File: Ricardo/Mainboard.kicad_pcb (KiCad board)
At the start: 4 copper layers, 100 x 60 mm, 326 parts, among them J1 USB_B_Micro, J10 Conn_01x02_Male, J11 Conn_01x02_Male, J12 Conn_01x02_Male, J2 8P8C_LED, J3 Micro_SD_Card_Det, J4 Conn_Coaxial, J5 Conn_Coaxial, J6 Screw_Terminal_01x02, J7 Screw_Terminal_01x02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

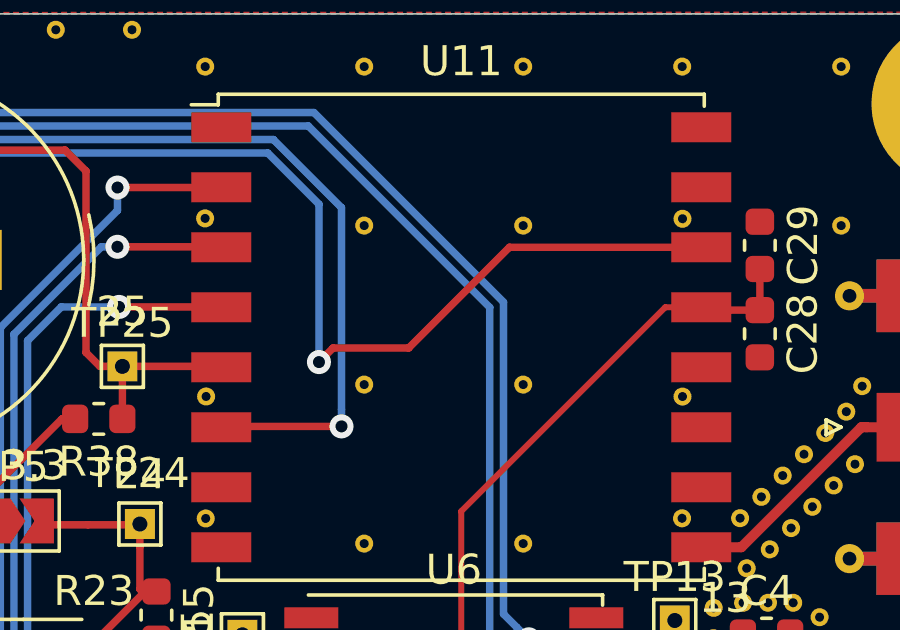
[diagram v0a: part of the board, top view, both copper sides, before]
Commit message: Added mit logo to ricardo board. added wipe functionality to storage controller
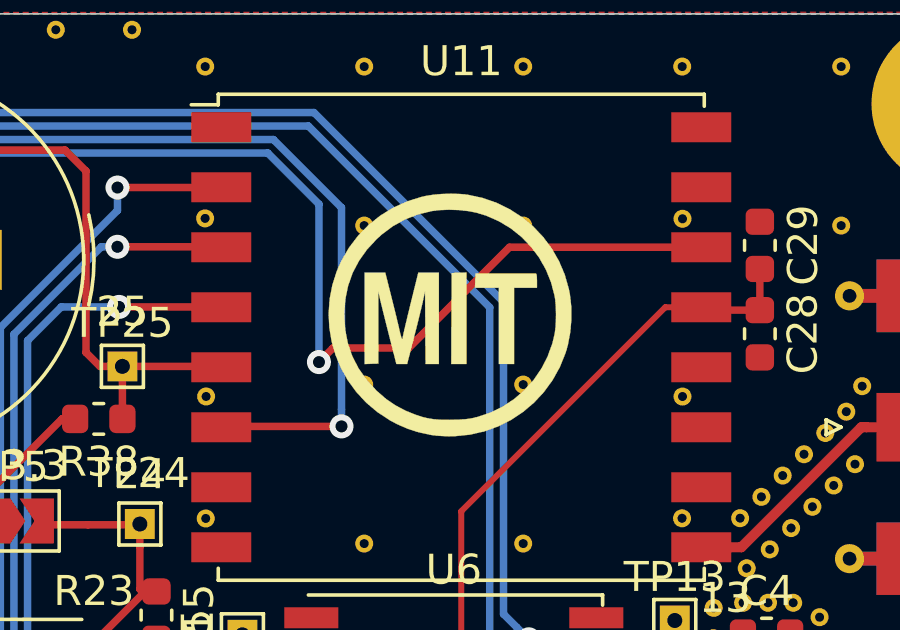
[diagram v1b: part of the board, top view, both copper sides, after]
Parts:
- added G***: LOGO, iclr-hw:MIT_logo, F.Cu at (165.2, 60.0)
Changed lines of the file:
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@@
     (tracks 1316)
     (zones 0)
-    (modules 326)
+    (modules 327)
     (nets 144)
   )
@@
     (uvia_drill 0.1)
   )
+  (module iclr-hw:MIT_logo (layer F.Cu)
+    (at 165.16 60.02)
+    (fp_text reference G*** (at 0 0) (layer F.SilkS) hide
+      (effects (font (size 1.524 1.524) (thickness 0.3)))
+    )
+    (fp_text value LOGO (at -0.05 5.77) (layer F.SilkS) hide
+      (effects (font (size 1.524 1.524) (thickness 0.3)))
+    )
+    (fp_poly (pts (xy 1.833562 -1.366762) (xy 2.079108 -1.366608) (xy 2.304556 -1.36644) (xy 2.501975 -1.366266)
+      (xy 2.663434 -1.366093) (xy 2.781 -1.36593) (xy 2.846742 -1.365785) (xy 2.8575 -1.365724)
+      (xy 2.873462 -1.335939) (xy 2.884619 -1.255889) (xy 2.889217 -1.138736) (xy 2.88925 -1.127125)
+      (xy 2.88925 -0.889) (xy 2.12725 -0.889) (xy 2.12725 1.651) (xy 1.61925 1.651)
+      (xy 1.61925 -0.889) (xy 0.822828 -0.889) (xy 0.832101 -1.128163) (xy 0.841375 -1.367325)
+      (xy 1.833562 -1.366762)) (layer F.SilkS) (width 0.01))
+    (fp_poly (pts (xy 0.53975 1.651) (xy 0.031134 1.651) (xy 0.039379 0.134937) (xy 0.047625 -1.381125)
+      (xy 0.293687 -1.390399) (xy 0.53975 -1.399672) (xy 0.53975 1.651)) (layer F.SilkS) (width 0.01))
+    (fp_poly (pts (xy -0.723536 -1.397) (xy -0.381 -1.397) (xy -0.381 1.651) (xy -0.824746 1.651)
+      (xy -0.833061 0.436562) (xy -0.841375 -0.777875) (xy -0.909244 -0.460375) (xy -0.935357 -0.344657)
+      (xy -0.974623 -0.179146) (xy -1.024176 0.0245) (xy -1.081154 0.254628) (xy -1.142694 0.499581)
+      (xy -1.205934 0.747703) (xy -1.207567 0.754062) (xy -1.438022 1.651) (xy -1.797534 1.651)
+      (xy -2.042334 0.690562) (xy -2.106115 0.439322) (xy -2.167533 0.195524) (xy -2.224052 -0.030632)
+      (xy -2.273139 -0.228944) (xy -2.312259 -0.389211) (xy -2.338878 -0.50123) (xy -2.34404 -0.523875)
+      (xy -2.400948 -0.777875) (xy -2.399037 0.428625) (xy -2.397125 1.635125) (xy -2.627313 1.644453)
+      (xy -2.8575 1.653781) (xy -2.8575 -1.397) (xy -2.167897 -1.397) (xy -1.953853 -0.547688)
+      (xy -1.894471 -0.310563) (xy -1.837603 -0.080676) (xy -1.78593 0.130918) (xy -1.742133 0.313163)
+      (xy -1.708895 0.455007) (xy -1.690063 0.53975) (xy -1.659757 0.669292) (xy -1.631356 0.763619)
+      (xy -1.607866 0.815801) (xy -1.592292 0.818904) (xy -1.58752 0.776287) (xy -1.580113 0.731638)
+      (xy -1.559064 0.632992) (xy -1.526149 0.487956) (xy -1.48314 0.304133) (xy -1.431812 0.089128)
+      (xy -1.373939 -0.149454) (xy -1.326806 -0.341313) (xy -1.066072 -1.397001) (xy -0.723536 -1.397)) (layer F.SilkS) (width 0.01))
+    (fp_poly (pts (xy 0.319577 -4.016704) (xy 0.57754 -3.991174) (xy 0.589705 -3.989348) (xy 1.080211 -3.88321)
+      (xy 1.546617 -3.720879) (xy 1.985107 -3.506085) (xy 2.391865 -3.242561) (xy 2.763073 -2.934037)
+      (xy 3.094917 -2.584246) (xy 3.383579 -2.196918) (xy 3.625244 -1.775785) (xy 3.816096 -1.324579)
+      (xy 3.952318 -0.84703) (xy 3.987706 -0.66675) (xy 4.033388 -0.257684) (xy 4.036025 0.173336)
+      (xy 3.997107 0.606492) (xy 3.918123 1.021965) (xy 3.840837 1.288573) (xy 3.650674 1.755648)
+      (xy 3.409658 2.188464) (xy 3.122002 2.584018) (xy 2.791919 2.939307) (xy 2.423622 3.251329)
+      (xy 2.021322 3.517079) (xy 1.589233 3.733555) (xy 1.131567 3.897754) (xy 0.652537 4.006673)
+      (xy 0.156355 4.057309) (xy -0.047625 4.060557) (xy -0.222552 4.055179) (xy -0.404296 4.043267)
+      (xy -0.565288 4.02688) (xy -0.635 4.016705) (xy -1.045097 3.929237) (xy -1.418609 3.810782)
+      (xy -1.778169 3.653278) (xy -2.020116 3.52328) (xy -2.436011 3.249745) (xy -2.807948 2.934222)
+      (xy -3.134438 2.581634) (xy -3.413992 2.196905) (xy -3.64512 1.78496) (xy -3.826334 1.350721)
+      (xy -3.956145 0.899114) (xy -4.033064 0.435061) (xy -4.052337 0.03175) (xy -3.532943 0.03175)
+      (xy -3.50245 0.508677) (xy -3.414685 0.958777) (xy -3.26904 1.383456) (xy -3.064905 1.784118)
+      (xy -2.801672 2.162168) (xy -2.478732 2.51901) (xy -2.43764 2.558845) (xy -2.138278 2.818013)
+      (xy -1.824742 3.032351) (xy -1.480521 3.21193) (xy -1.1459 3.34677) (xy -0.934756 3.41556)
+      (xy -0.733107 3.464313) (xy -0.524236 3.495268) (xy -0.291425 3.510669) (xy -0.017955 3.512754)
+      (xy 0.079375 3.51101) (xy 0.298106 3.504232) (xy 0.470868 3.493788) (xy 0.615165 3.477699)
+      (xy 0.748505 3.453988) (xy 0.888396 3.420678) (xy 0.895534 3.418815) (xy 1.337238 3.271201)
+      (xy 1.750323 3.06936) (xy 2.130777 2.817604) (xy 2.474586 2.520247) (xy 2.777734 2.181601)
+      (xy 3.03621 1.805979) (xy 3.245997 1.397692) (xy 3.403084 0.961055) (xy 3.479141 0.642924)
+      (xy 3.504097 0.457375) (xy 3.518555 0.230965) (xy 3.522516 -0.014541) (xy 3.515979 -0.257376)
+      (xy 3.498945 -0.475775) (xy 3.479141 -0.611175) (xy 3.36101 -1.065244) (xy 3.187357 -1.493887)
+      (xy 2.962179 -1.892808) (xy 2.689476 -2.257709) (xy 2.373249 -2.584293) (xy 2.017495 -2.868263)
+      (xy 1.626215 -3.105322) (xy 1.203407 -3.291171) (xy 0.895534 -3.387263) (xy 0.6052 -3.445365)
+      (xy 0.279262 -3.480157) (xy -0.058472 -3.490736) (xy -0.384192 -3.476202) (xy -0.625874 -3.444865)
+      (xy -1.085496 -3.33254) (xy -1.514784 -3.16484) (xy -1.916038 -2.940591) (xy -2.291557 -2.658623)
+      (xy -2.450639 -2.51462) (xy -2.777185 -2.162444) (xy -3.045148 -1.785778) (xy -3.254605 -1.384434)
+      (xy -3.405636 -0.958226) (xy -3.498321 -0.506967) (xy -3.532738 -0.030473) (xy -3.532943 0.03175)
+      (xy -4.052337 0.03175) (xy -4.0556 -0.036513) (xy -4.022266 -0.510684) (xy -3.931572 -0.982529)
+      (xy -3.78203 -1.447124) (xy -3.627841 -1.792857) (xy -3.372441 -2.231357) (xy -3.069511 -2.629503)
+      (xy -2.722748 -2.984458) (xy -2.335854 -3.293387) (xy -1.912529 -3.553454) (xy -1.456471 -3.761822)
+      (xy -0.971381 -3.915656) (xy -0.809625 -3.953113) (xy -0.560393 -3.992633) (xy -0.273225 -4.016816)
+      (xy 0.028044 -4.025045) (xy 0.319577 -4.016704)) (layer F.SilkS) (width 0.01))
+  )
   (module Package_TO_SOT_SMD:SOT-23-5 (layer F.Cu)
